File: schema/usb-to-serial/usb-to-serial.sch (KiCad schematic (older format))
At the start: 36 parts, among them P1 CONN_6X2, Q1 MOS_P, U1 FT232BL, U2 LP5951MF-3.3, U3 MINI-USB-B, X1 CRYSTAL

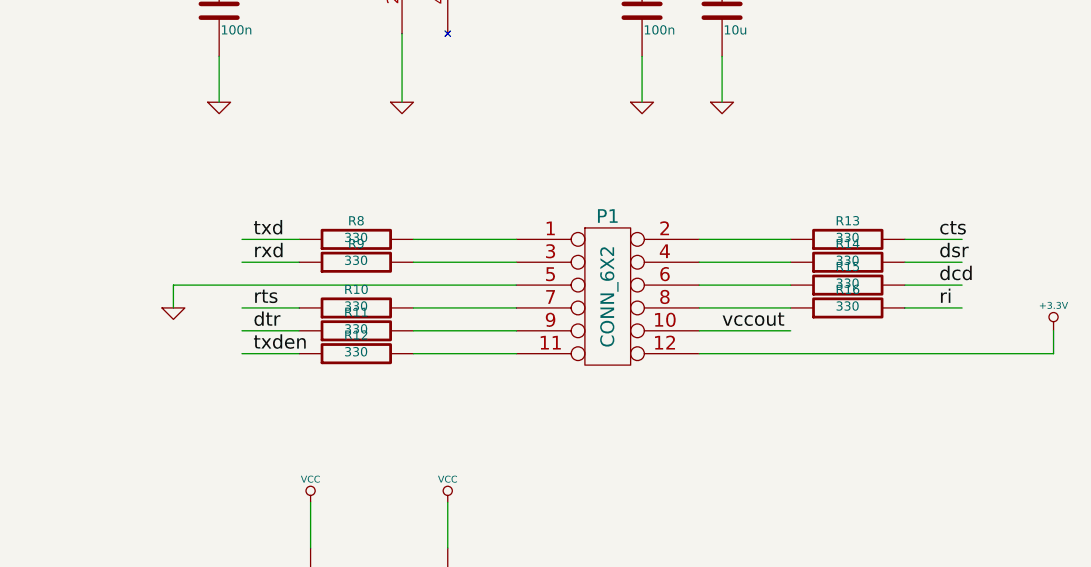
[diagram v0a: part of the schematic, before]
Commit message: Changed scheme for easier routing.
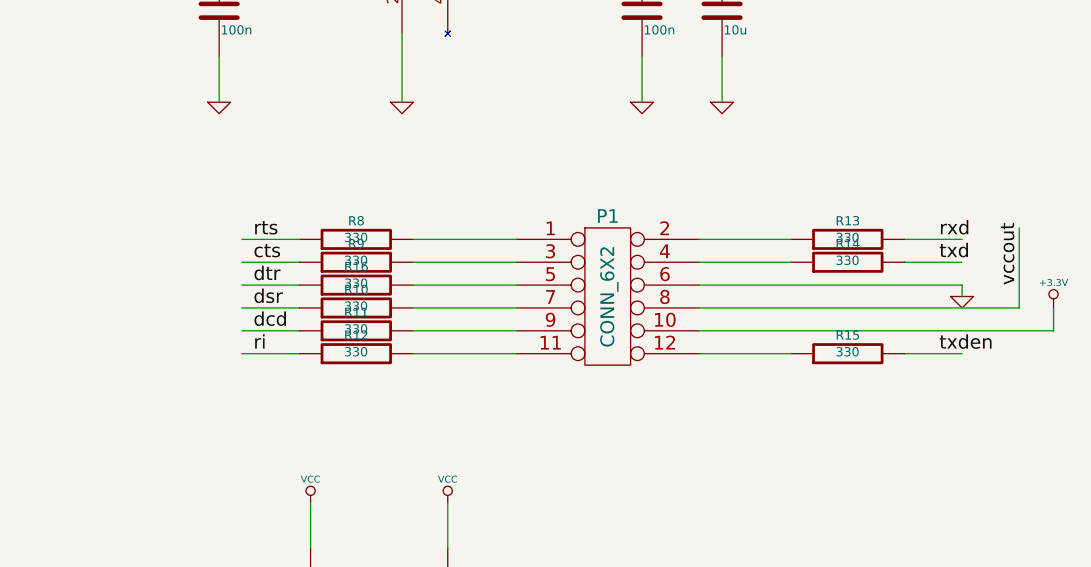
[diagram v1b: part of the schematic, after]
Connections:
- wire segments 120 -> 121
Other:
- moved on the sheet: R15
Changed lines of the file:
@@
-EESchema Schematic File Version 2  date Sat 13 Apr 2013 12:53:10 AM MSK
+EESchema Schematic File Version 2  date Sat 13 Apr 2013 11:18:08 PM MSK
 LIBS:power
 LIBS:device
@@
 Sheet 1 1
 Title ""
-Date "12 apr 2013"
+Date "13 apr 2013"
 Rev ""
 Comp ""
@@
 	12700 3300 12250 3300
 Wire Wire Line
-	11200 3400 12700 3400
-Wire Wire Line
 	12700 3500 12250 3500
 Wire Wire Line
@@
 	13500 3300 13900 3300
 Wire Wire Line
-	13500 3400 13900 3400
-Wire Wire Line
-	13500 3500 13900 3500
-Wire Wire Line
-	13500 3700 15050 3700
+	13500 3700 13900 3700
+Wire Wire Line
+	13500 3600 15050 3600
+Text Label 14550 3300 0    60   ~ 0
+txd
+Text Label 14550 3200 0    60   ~ 0
+rxd
 Text Label 11550 3200 0    60   ~ 0
-txd
+rts
+Text Label 11550 3400 0    60   ~ 0
+dtr
+Text Label 14550 3700 0    60   ~ 0
+txden
 Text Label 11550 3300 0    60   ~ 0
-rxd
+cts
 Text Label 11550 3500 0    60   ~ 0
-rts
+dsr
 Text Label 11550 3600 0    60   ~ 0
-dtr
+dcd
 Text Label 11550 3700 0    60   ~ 0
-txden
-Text Label 14550 3200 0    60   ~ 0
-cts
-Text Label 14550 3300 0    60   ~ 0
-dsr
-Text Label 14550 3400 0    60   ~ 0
-dcd
-Text Label 14550 3500 0    60   ~ 0
 ri
 NoConn ~ 7250 5800
@@
 L +3.3V #PWR027
 U 1 1 51687636
-P 15050 3600
-F 0 "#PWR027" H 15050 3560 30  0001 C CNN
-F 1 "+3.3V" H 15050 3710 30  0000 C CNN
-F 2 "" H 15050 3600 60  0000 C CNN
-F 3 "" H 15050 3600 60  0000 C CNN
-	1    15050 3600
+P 15050 3500
+F 0 "#PWR027" H 15050 3460 30  0001 C CNN
+F 1 "+3.3V" H 15050 3610 30  0000 C CNN
+F 2 "" H 15050 3500 60  0000 C CNN
+F 3 "" H 15050 3500 60  0000 C CNN
+	1    15050 3500
 	1    0    0    -1
 $EndComp
@@
 Text Label 12900 6700 0    60   ~ 0
 vccout
-Text Label 13600 3600 0    60   ~ 0
+Text Label 14900 3400 1    60   ~ 0
 vccout
 $Comp
@@
 Wire Wire Line
 	11750 3500 11500 3500
-Wire Wire Line
-	11200 3400 11200 3500
 $Comp
 L GND #PWR037
 U 1 1 51688F1C
-P 11200 3500
-F 0 "#PWR037" H 11200 3500 30  0001 C CNN
-F 1 "GND" H 11200 3430 30  0001 C CNN
-F 2 "" H 11200 3500 60  0000 C CNN
-F 3 "" H 11200 3500 60  0000 C CNN
-	1    11200 3500
+P 14650 3450
+F 0 "#PWR037" H 14650 3450 30  0001 C CNN
+F 1 "GND" H 14650 3380 30  0001 C CNN
+F 2 "" H 14650 3450 60  0000 C CNN
+F 3 "" H 14650 3450 60  0000 C CNN
+	1    14650 3450
 	1    0    0    -1
 $EndComp
@@
 L R R15
 U 1 1 51688F3C
-P 14150 3400
-F 0 "R15" V 14230 3400 40  0000 C CNN
-F 1 "330" V 14157 3401 40  0000 C CNN
-F 2 "~" V 14080 3400 30  0000 C CNN
-F 3 "~" H 14150 3400 30  0000 C CNN
-	1    14150 3400
+P 14150 3700
+F 0 "R15" V 14230 3700 40  0000 C CNN
+F 1 "330" V 14157 3701 40  0000 C CNN
+F 2 "~" V 14080 3700 30  0000 C CNN
+F 3 "~" H 14150 3700 30  0000 C CNN
+	1    14150 3700
 	0    -1   -1   0
 $EndComp
-$Comp
-L R R16
-U 1 1 51688F42
-P 14150 3500
-F 0 "R16" V 14230 3500 40  0000 C CNN
-F 1 "330" V 14157 3501 40  0000 C CNN
-F 2 "~" V 14080 3500 30  0000 C CNN
-F 3 "~" H 14150 3500 30  0000 C CNN
-	1    14150 3500
-	0    -1   -1   0
-$EndComp
-Wire Wire Line
-	15050 3700 15050 3600
-Wire Wire Line
-	14400 3500 14650 3500
-Wire Wire Line
-	14400 3400 14650 3400
+Wire Wire Line
+	15050 3600 15050 3500
+Wire Wire Line
+	14400 3700 14650 3700
 Wire Wire Line
 	14400 3300 14650 3300
 Wire Wire Line
 	14400 3200 14650 3200
-Wire Wire Line
-	13900 3600 13500 3600
 $Comp
 L MINI-USB-B U3
@@
 	1    0    0    -1
 $EndComp
+$Comp
+L R R16
+U 1 1 5169AE8D
+P 12000 3400
+F 0 "R16" V 12080 3400 40  0000 C CNN
+F 1 "330" V 12007 3401 40  0000 C CNN
+F 2 "~" V 11930 3400 30  0000 C CNN
+F 3 "~" H 12000 3400 30  0000 C CNN
+	1    12000 3400
+	0    -1   -1   0
+$EndComp
+Wire Wire Line
+	12700 3400 12250 3400
+Wire Wire Line
+	11750 3400 11500 3400
+Wire Wire Line
+	13500 3400 14650 3400
+Wire Wire Line
+	14650 3400 14650 3450
+Wire Wire Line
+	13500 3500 14900 3500
+Wire Wire Line
+	14900 3500 14900 3150
 $EndSCHEMATC
